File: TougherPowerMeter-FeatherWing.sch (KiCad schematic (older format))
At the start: 40 parts, among them J1 Jumper, J10 796639-2, J11 Jumper, J2 796639-2, J3 796639-2, J4 796639-2, J5 796639-2, J6 796639-2, J7 796639-2, J8 796639-2, J9 796639-2, U1 AP63205, U2 TPS1HB08A-Q1, U3 FeatherWing, U4 INA3221

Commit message: Finish design
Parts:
- removed C2, C6: 220n, Capacitor_SMD:C_0603_1608Metric, symbol Device:C_Small
- removed C3, C4: 100n, Resistor_SMD:R_0603_1608Metric, symbol Device:C_Small
- removed C5, C7: 22u, Capacitor_SMD:C_0805_2012Metric, symbol Device:C_Small
- removed L1: 4.7u, Inductor_SMD_BD:L_Bourns_SRR1210A, symbol Device:L
- removed R3, R4, R5, R6, R7: 10k, Resistor_SMD:R_0603_1608Metric, symbol Device:R_Small
- removed U1: AP63205, Package_TO_SOT_SMD:TSOT-23-6, symbol Power_Management_BD:AP63205
- removed U2: TPS1HB08A-Q1, Package_SO:HTSSOP-16-1EP_4.4x5mm_P0.65mm_EP3.4x5mm, symbol Power_Management_BD:TPS1HB08-Q1
- added A1: Arduino_Nano_v3.x, Module_BD:Arduino_Nano_NoSilk, symbol MCU_Module:Arduino_Nano_v3.x
- added C18: 4.7uF, Capacitor_SMD:C_0603_1608Metric, symbol Device:C_Small
- added H1, H2, H3, H4: MountingHole, MountingHole:MountingHole_3.2mm_M3_Pad_Via, symbol Mechanical:MountingHole
- C1: value 10u -> 4.7uF; footprint Capacitor_SMD:C_1206_3216Metric -> Capacitor_SMD:C_0603_1608Metric; Voltage 35V -> (none)
- R2: value 12k -> 220
- U3: footprint Module_BD:FeatherWing -> Module_BD:FeatherWing_NoMH
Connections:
- net +3V3: now also C1.1, R8.1, U4.16 (VPU), A1.17 (3V3), C18.1
- net +5V: now also U3.26 (VBUS), A1.30 (VIN); no longer J1.2 (Pin_2)
- net CH1_IN: now also J2.1 (Pin_1); no longer J2.2 (Pin_2)
- net CH1_OUT: now also J1.1 (Pin_1), J5.1 (Pin_1), J8.1 (Pin_1); no longer C1.2, J5.2 (Pin_2), J8.2 (Pin_2)
- net CH2_IN: now also J3.1 (Pin_1); no longer J3.2 (Pin_2)
- net CH2_OUT: now also J6.1 (Pin_1), J9.1 (Pin_1); no longer J6.2 (Pin_2), J9.2 (Pin_2)
- net CH3_DIA_EN: now also A1.19 (A0)
- net CH3_EN: now also A1.7 (D4)
- net CH3_IN: now also J4.1 (Pin_1); no longer J4.2 (Pin_2), R2.2
- net CH3_LATCH: now also A1.6 (D3)
- net CH3_OUT: now also J10.1 (Pin_1), J7.1 (Pin_1); no longer J10.2 (Pin_2), J7.2 (Pin_2)
- net CH3_SEL: now also A1.5 (D2)
- net CH3_SNS: now also A1.20 (A1)
- net CRITICAL: now also A1.10 (D7)
- net GND: now also C1.2, J10.2 (Pin_2), J2.2 (Pin_2), J3.2 (Pin_2), J4.2 (Pin_2), J5.2 (Pin_2), J6.2 (Pin_2), J7.2 (Pin_2), J8.2 (Pin_2), J9.2 (Pin_2), A1.29 (GND), A1.4 (GND), C18.2; no longer C1.1, J10.1 (Pin_1), J2.1 (Pin_1), J3.1 (Pin_1), J4.1 (Pin_1), J5.1 (Pin_1), J6.1 (Pin_1), J7.1 (Pin_1), J8.1 (Pin_1), J9.1 (Pin_1), R1.1
- net POWER_VALID: now also A1.11 (D8)
- net SCL: now also R2.1, A1.24 (A5); no longer R10.2, U4.6 (SCL)
- net SDA: now also R1.1, A1.25 (A6); no longer R9.2, U4.7 (SDA)
- net TIMING_CTRL: now also A1.8 (D5)
- net WARNING: now also A1.9 (D6)
- net at R1.2: now also R9.2, U4.7 (SDA)
- net current-sense-frontend-CH1/IS+ renamed IN1_P
- net current-sense-frontend-CH1/IS- renamed IN1_N
- net current-sense-frontend-CH2/IS+ renamed IN2_P
- net current-sense-frontend-CH2/IS- renamed IN2_N
- net current-sense-frontend-CH3/IS+ renamed IN3_P
- net current-sense-frontend-CH3/IS- renamed IN3_N
- new net: R10.2, R2.2, U4.6 (SCL)
- new net buck/VIN: J1.2 (Pin_2)
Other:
- note removed: "500mA \ncontinuous max"
- note removed: "@R2=12k\nMinimal current limit 10A\nTypical current limit 13.3A\nMaximum current limit 17.3A"
- note removed: "Channel 1 is connected to a buck converter \nto provide 5V for the Feather.\nDisconnect J1 jumper if Feather has external power."
- note removed: "Current limit is set by R2\nIlim = K / R2\nKmin = 120\nKtyp = 160\nKmax = 208"
- note removed: "Disconnect the jumper\nif Feather is powered from USB,\nto prevent back-powering."
- moved on the sheet: C8, J11, R13, R14, R8, U3

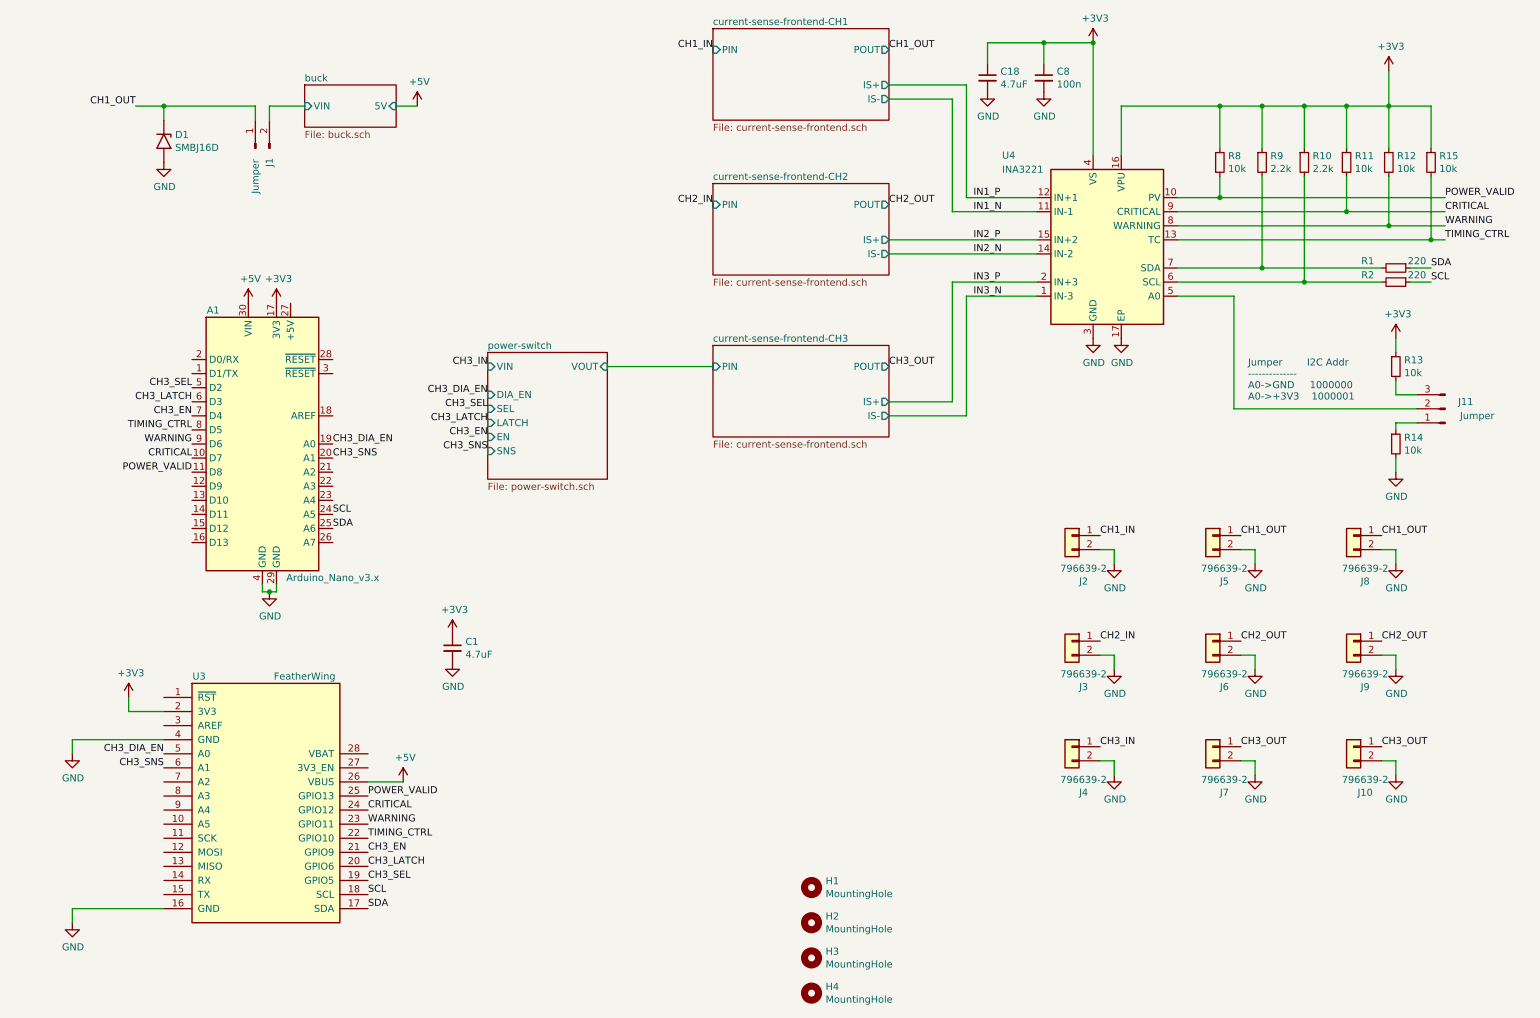
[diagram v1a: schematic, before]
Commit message: Add fiducials, fix aesthetics in schematics
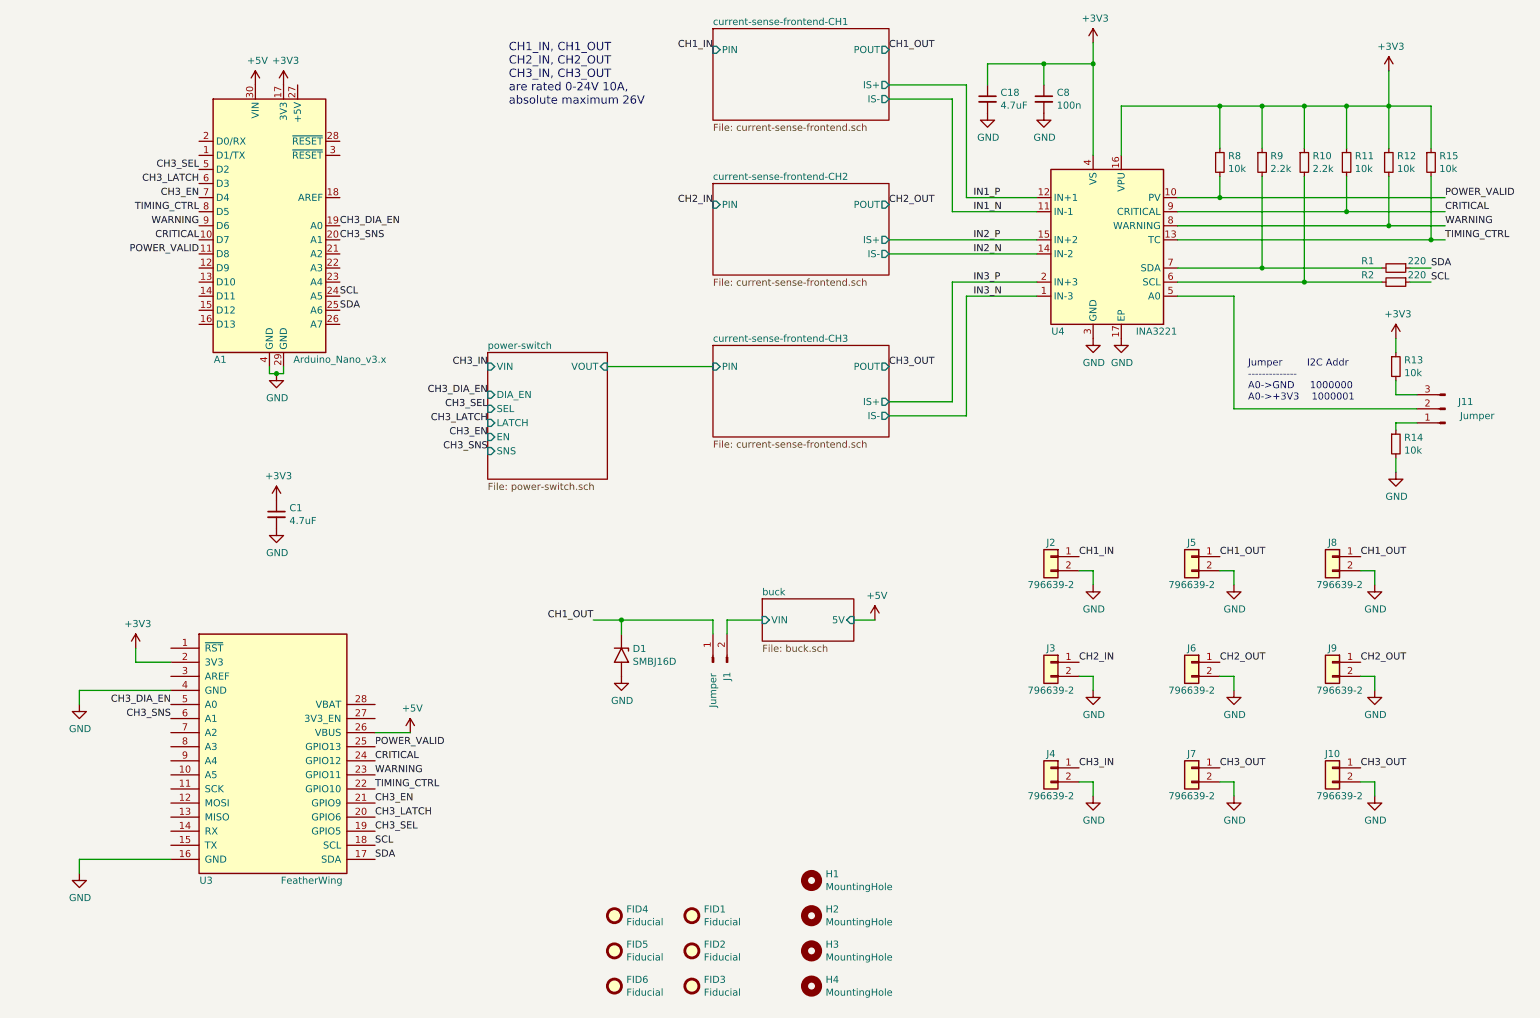
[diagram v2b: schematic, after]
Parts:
- added FID1, FID2, FID3, FID4, FID5, FID6: Fiducial, Fiducial:Fiducial_1.5mm_Mask4.5mm, symbol Mechanical:Fiducial
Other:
- note added: "CH1_IN, CH1_OUT\nCH2_IN, CH2_OUT\nCH3_IN, CH3_OUT\nare rated 0-24V 10A,\nabsolute maximum 26V"
- moved on the sheet: A1, C1, C18, C8, D1, H1, H2, H3, H4, J1, J10, J2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

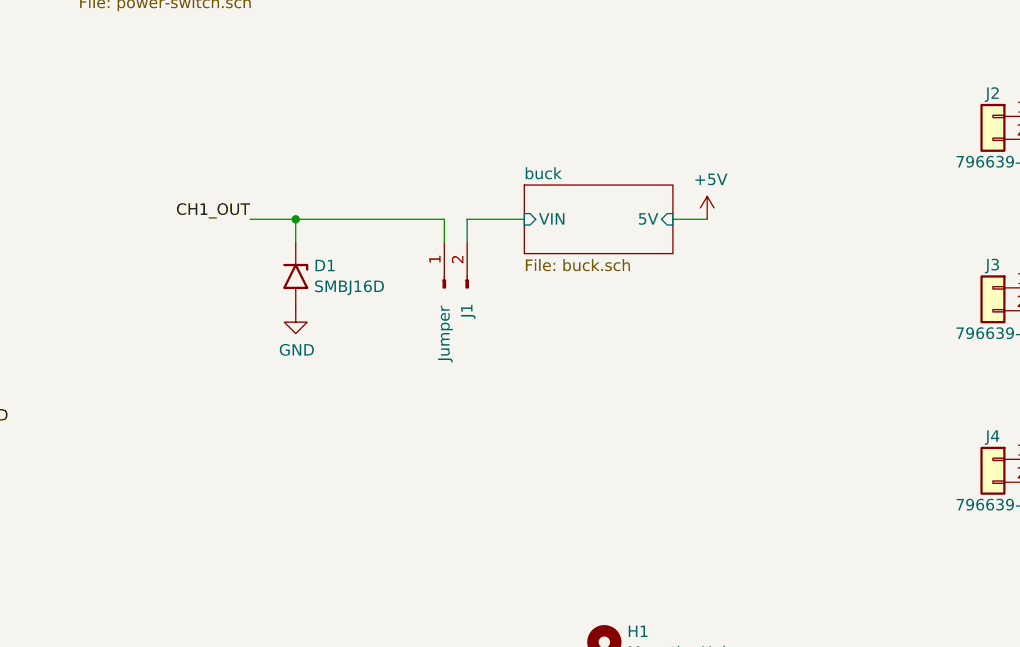
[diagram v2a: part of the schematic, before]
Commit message: Add comment to schematics:
CH1 can be used to power Arduino or Feather via
a buck converter. Disconnect jumper J1 if Arduino
or Feather have their own separate power.
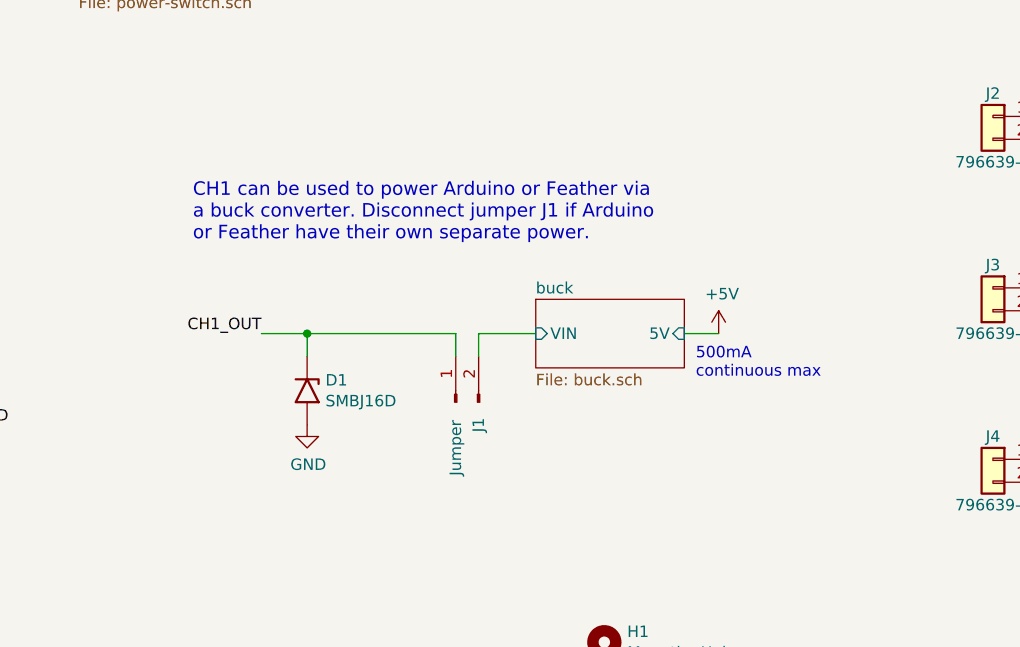
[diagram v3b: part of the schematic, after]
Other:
- note added: "500mA \ncontinuous max"
- note added: "CH1 can be used to power Arduino or Feather via \na buck converter. Disconnect jumper J1 if Arduino \nor Feather have their own separate power."
- moved on the sheet: D1, J1
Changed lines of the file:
@@
 	10450 2550 10600 2550
 $Sheet
-S 5850 4800 650  300
+S 5900 5300 650  300
 U 5F5E3585
 F0 "buck" 50
 F1 "buck.sch" 50
-F2 "5V" I R 6500 4950 50
-F3 "VIN" I L 5850 4950 50
+F2 "5V" I R 6550 5450 50
+F3 "VIN" I L 5900 5450 50
 $EndSheet
 $Comp
 L Connector:Conn_01x02_Male J1
 U 1 1 5F602226
-P 5500 5250
-F 0 "J1" H 5400 5150 50  0000 C CNN
-F 1 "Jumper" H 5300 5250 50  0000 C CNN
-F 2 "Connector_PinHeader_2.54mm:PinHeader_1x02_P2.54mm_Vertical" H 5500 5250 50  0001 C CNN
-F 3 "~" H 5500 5250 50  0001 C CNN
-	1    5500 5250
+P 5550 5750
+F 0 "J1" H 5450 5650 50  0000 C CNN
+F 1 "Jumper" H 5350 5750 50  0000 C CNN
+F 2 "Connector_PinHeader_2.54mm:PinHeader_1x02_P2.54mm_Vertical" H 5550 5750 50  0001 C CNN
+F 3 "~" H 5550 5750 50  0001 C CNN
+	1    5550 5750
 	0    -1   -1   0
 $EndComp
-Text Label 4650 4950 2    50   ~ 0
+Text Label 4700 5450 2    50   ~ 0
 CH1_OUT
 $Comp
 L power:+5V #PWR0105
 U 1 1 5F623654
-P 6650 4950
-F 0 "#PWR0105" H 6650 4800 50  0001 C CNN
-F 1 "+5V" H 6665 5123 50  0000 C CNN
-F 2 "" H 6650 4950 50  0001 C CNN
-F 3 "" H 6650 4950 50  0001 C CNN
-	1    6650 4950
-	1    0    0    -1
-$EndComp
-Wire Wire Line
-	6500 4950 6650 4950
-Wire Wire Line
-	4650 4950 4850 4950
-Wire Wire Line
-	5500 4950 5500 5050
-Wire Wire Line
-	5600 5050 5600 4950
-Wire Wire Line
-	5600 4950 5850 4950
+P 6700 5450
+F 0 "#PWR0105" H 6700 5300 50  0001 C CNN
+F 1 "+5V" H 6715 5623 50  0000 C CNN
+F 2 "" H 6700 5450 50  0001 C CNN
+F 3 "" H 6700 5450 50  0001 C CNN
+	1    6700 5450
+	1    0    0    -1
+$EndComp
+Wire Wire Line
+	6550 5450 6700 5450
+Wire Wire Line
+	4700 5450 4900 5450
+Wire Wire Line
+	5550 5450 5550 5550
+Wire Wire Line
+	5650 5550 5650 5450
+Wire Wire Line
+	5650 5450 5900 5450
 $Sheet
 S 3900 3050 850  900
@@
 CH3_DIA_EN
 Wire Wire Line
-	4850 4950 4850 5050
+	4900 5450 4900 5550
 $Comp
 L Diodes:SMBJxxxD D?
 U 1 1 5F6B0AA1
-P 4850 5200
+P 4900 5700
 AR Path="/5F41030B/5F6B0AA1" Ref="D?"  Part="1"
 AR Path="/5F4101BA/5F6B0AA1" Ref="D?"  Part="1"
@@
 AR Path="/5F6B0AA1" Ref="D1"  Part="1"
 AR Path="/5F5E3585/5F6B0AA1" Ref="D?"  Part="1"
-F 0 "D1" V 4804 5280 50  0000 L CNN
-F 1 "SMBJ16D" V 4895 5280 50  0000 L CNN
-F 2 "Diode_SMD:D_SMB" H 4850 5000 50  0001 C CNN
-F 3 "https://www.vishay.com/docs/87606/smbj5cdthrusmbj120cd.pdf" H 4800 5200 50  0001 C CNN
-	1    4850 5200
+F 0 "D1" V 4854 5780 50  0000 L CNN
+F 1 "SMBJ16D" V 4945 5780 50  0000 L CNN
+F 2 "Diode_SMD:D_SMB" H 4900 5500 50  0001 C CNN
+F 3 "https://www.vishay.com/docs/87606/smbj5cdthrusmbj120cd.pdf" H 4850 5700 50  0001 C CNN
+	1    4900 5700
 	0    1    1    0
 $EndComp
@@
 L power:GND #PWR?
 U 1 1 5F6B0AA7
-P 4850 5350
+P 4900 5850
 AR Path="/5F404FBF/5F6B0AA7" Ref="#PWR?"  Part="1"
 AR Path="/5F41030B/5F6B0AA7" Ref="#PWR?"  Part="1"
@@
 AR Path="/5F6B0AA7" Ref="#PWR0112"  Part="1"
 AR Path="/5F5E3585/5F6B0AA7" Ref="#PWR?"  Part="1"
-F 0 "#PWR0112" H 4850 5100 50  0001 C CNN
-F 1 "GND" H 4855 5177 50  0000 C CNN
-F 2 "" H 4850 5350 50  0001 C CNN
-F 3 "" H 4850 5350 50  0001 C CNN
-	1    4850 5350
-	1    0    0    -1
-$EndComp
-Wire Wire Line
-	4850 4950 5500 4950
-Connection ~ 4850 4950
+F 0 "#PWR0112" H 4900 5600 50  0001 C CNN
+F 1 "GND" H 4905 5677 50  0000 C CNN
+F 2 "" H 4900 5850 50  0001 C CNN
+F 3 "" H 4900 5850 50  0001 C CNN
+	1    4900 5850
+	1    0    0    -1
+$EndComp
+Wire Wire Line
+	4900 5450 5550 5450
+Connection ~ 4900 5450
 $Comp
 L Device:C_Small C1
@@
 Text Notes 4050 1300 0    59   ~ 0
 CH1_IN, CH1_OUT\nCH2_IN, CH2_OUT\nCH3_IN, CH3_OUT\nare rated 0-24V 10A,\nabsolute maximum 26V
+Text Notes 4400 5050 0    59   ~ 0
+CH1 can be used to power Arduino or Feather via \na buck converter. Disconnect jumper J1 if Arduino \nor Feather have their own separate power.
+Text Notes 6600 5650 0    50   ~ 0
+500mA \ncontinuous max
 $EndSCHEMATC
